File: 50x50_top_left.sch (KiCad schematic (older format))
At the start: 90 parts, among them CON1 BARREL_JACK, CON2 USB_FEMALE_WITH_ID, CON3 USB_FEMALE_WITH_ID, J1 INTERCONNECT_1X03, J10 INTERCONNECT_1X03, J11 INTERCONNECT_1X03, J12 INTERCONNECT_1X03, J13 INTERCONNECT_1X03, J14 INTERCONNECT_1X03, J15 INTERCONNECT_1X03, J16 INTERCONNECT_1X03, J17 INTERCONNECT_1X03, J18 INTERCONNECT_1X03, J19 INTERCONNECT_1X03, J2 INTERCONNECT_1X03, J20 INTERCONNECT_1X03, J21 INTERCONNECT_1X03, J22 INTERCONNECT_1X03, J23 INTERCONNECT_1X03, J24 INTERCONNECT_1X03, J25 INTERCONNECT_1X03, J26 INTERCONNECT_1X03, J27 INTERCONNECT_1X03, J28 INTERCONNECT_1X03, J29 INTERCONNECT_1X03, J3 INTERCONNECT_1X03, J30 INTERCONNECT_1X03, J31 INTERCONNECT_1X03, J32 INTERCONNECT_1X03, J33 INTERCONNECT_1X03, J34 INTERCONNECT_1X03, J35 INTERCONNECT_1X03, J36 INTERCONNECT_1X03, J37 INTERCONNECT_1X03, J38 INTERCONNECT_1X03, J39 INTERCONNECT_1X03, J4 INTERCONNECT_1X03, J40 INTERCONNECT_1X03, J41 INTERCONNECT_1X03, J42 INTERCONNECT_1X03, J43 INTERCONNECT_1X03, J44 INTERCONNECT_1X03, J45 INTERCONNECT_1X03, J46 INTERCONNECT_1X03, J47 INTERCONNECT_1X03, J48 INTERCONNECT_1X03, J49 INTERCONNECT_1X03, J5 INTERCONNECT_1X03, J50 INTERCONNECT_1X03, J51 INTERCONNECT_1X03, J52 INTERCONNECT_1X03, J53 INTERCONNECT_1X03, J54 INTERCONNECT_1X03, J55 INTERCONNECT_1X03, J56 INTERCONNECT_1X03, J57 INTERCONNECT_1X03, J58 INTERCONNECT_1X03, J59 INTERCONNECT_1X03, J6 INTERCONNECT_1X03, J60 INTERCONNECT_1X03, J61 INTERCONNECT_1X03, J62 INTERCONNECT_1X03, J63 INTERCONNECT_1X03, J64 INTERCONNECT_1X03, J65 INTERCONNECT_1X02, J7 INTERCONNECT_1X03, J8 INTERCONNECT_1X03, J9 INTERCONNECT_1X03, P1 CONN_5, U1 LM7805CT

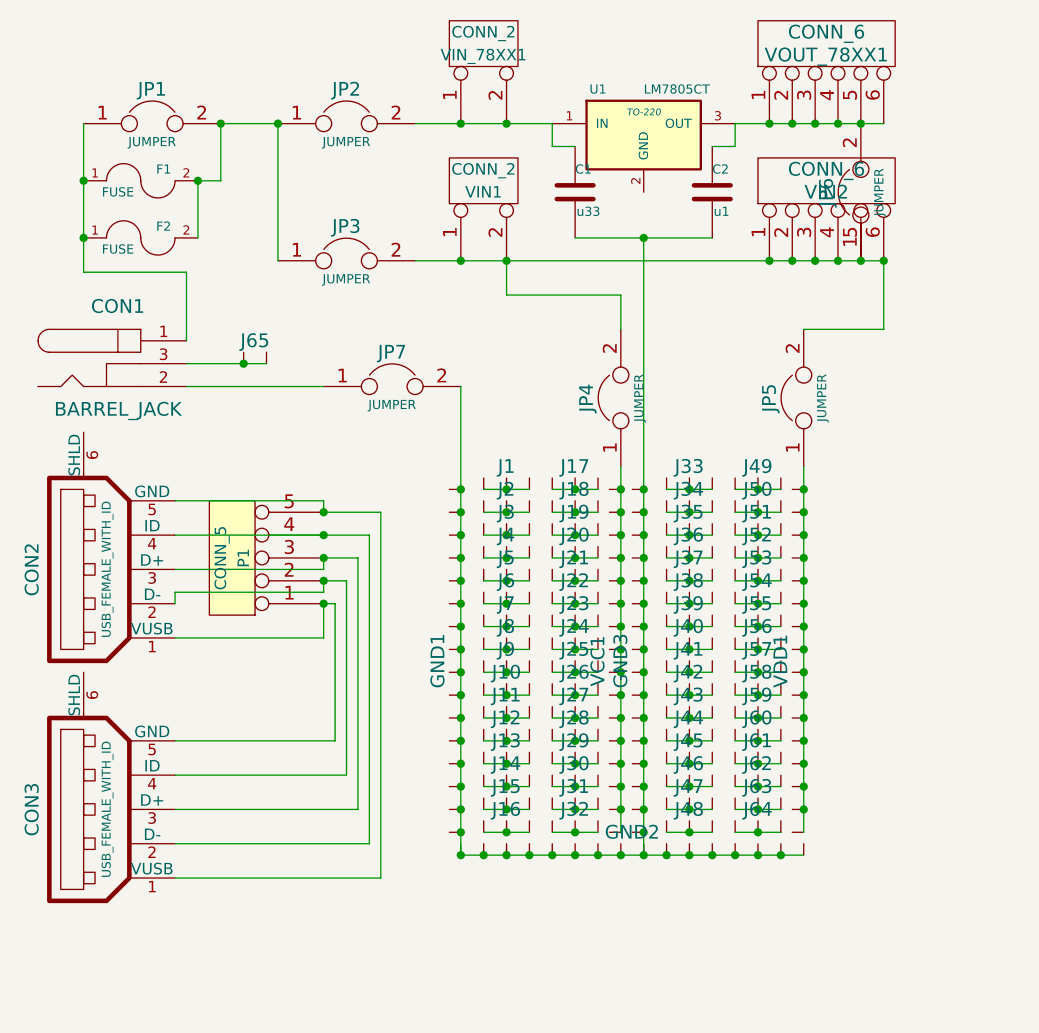
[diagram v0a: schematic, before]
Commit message: completed top-left corner
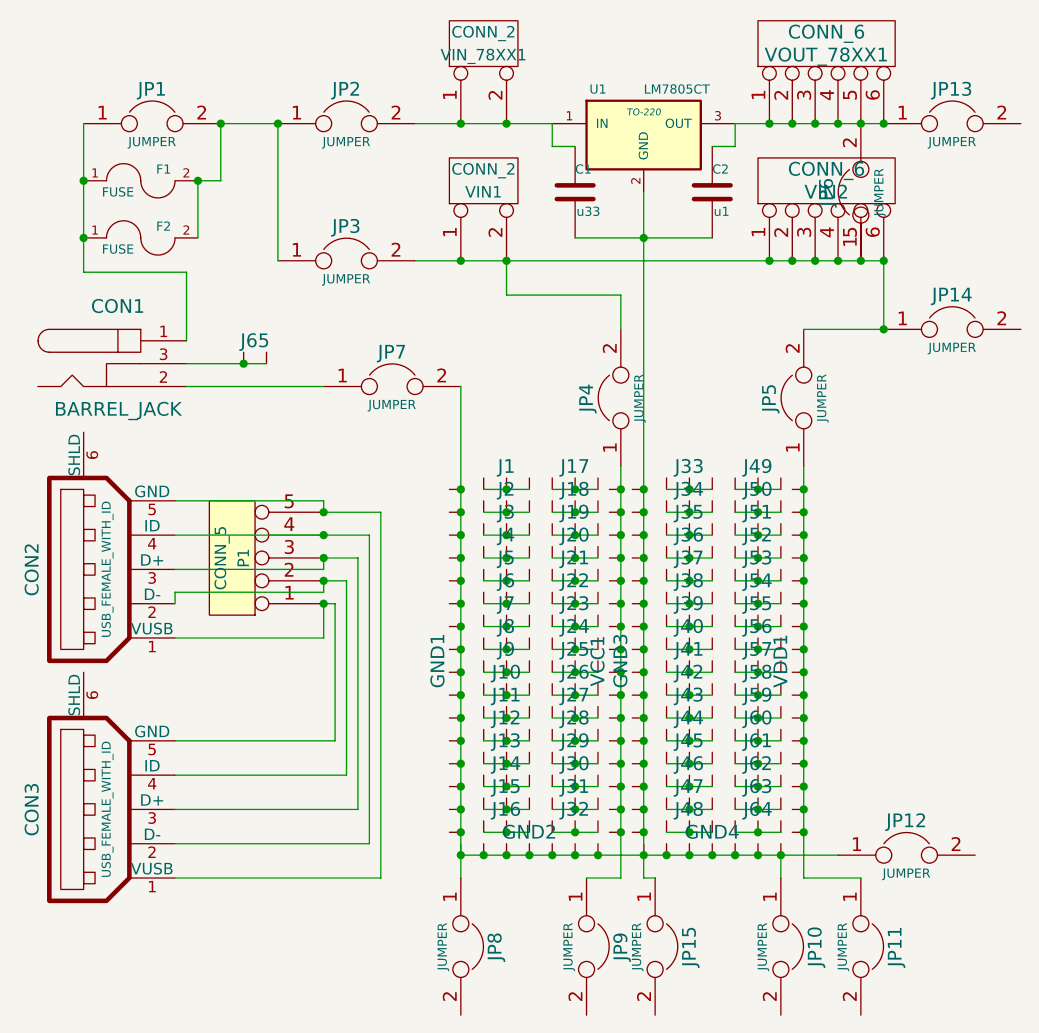
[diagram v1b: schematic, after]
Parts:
- removed GND2: INTERCONNECT_1X16, ~, symbol INTERCONNECT_1X16
- added GND2, GND4: INTERCONNECT_1X07, symbol INTERCONNECT_1X07
- added JP10, JP11, JP12, JP13, JP14, JP15, JP8, JP9: JUMPER, symbol JUMPER
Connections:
- net at C1.2, C2.2, GND1.1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: now also U1.2 (GND), GND2.1, GND4.1, JP10.1, JP12.1, JP15.1, JP8.1
- net at JP5.1, VDD1.1: now also JP11.1
- net at JP4.1, VCC1.1: now also JP9.1
- net at JP3.2, JP4.2, JP5.2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: now also JP14.1
- net at C2.1, JP6.2, U1.3 (OUT)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: now also JP13.1
